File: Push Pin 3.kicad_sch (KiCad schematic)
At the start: 27 parts, among them J1 Screw_Terminal_01x02, J10 Screw_Terminal_01x02, J11 Screw_Terminal_01x02, J12 Screw_Terminal_01x02, J13 Screw_Terminal_01x02, J4 Screw_Terminal_01x02, J5 Screw_Terminal_01x02, J6 Screw_Terminal_01x02, J7 Screw_Terminal_01x02, J8 Screw_Terminal_01x02, J9 Screw_Terminal_01x02, SW1 SW_DPDT_x2, SW2 SW_DPDT_x2, SW3 SW_DPDT_x2, U1 LM2596S-ADJ

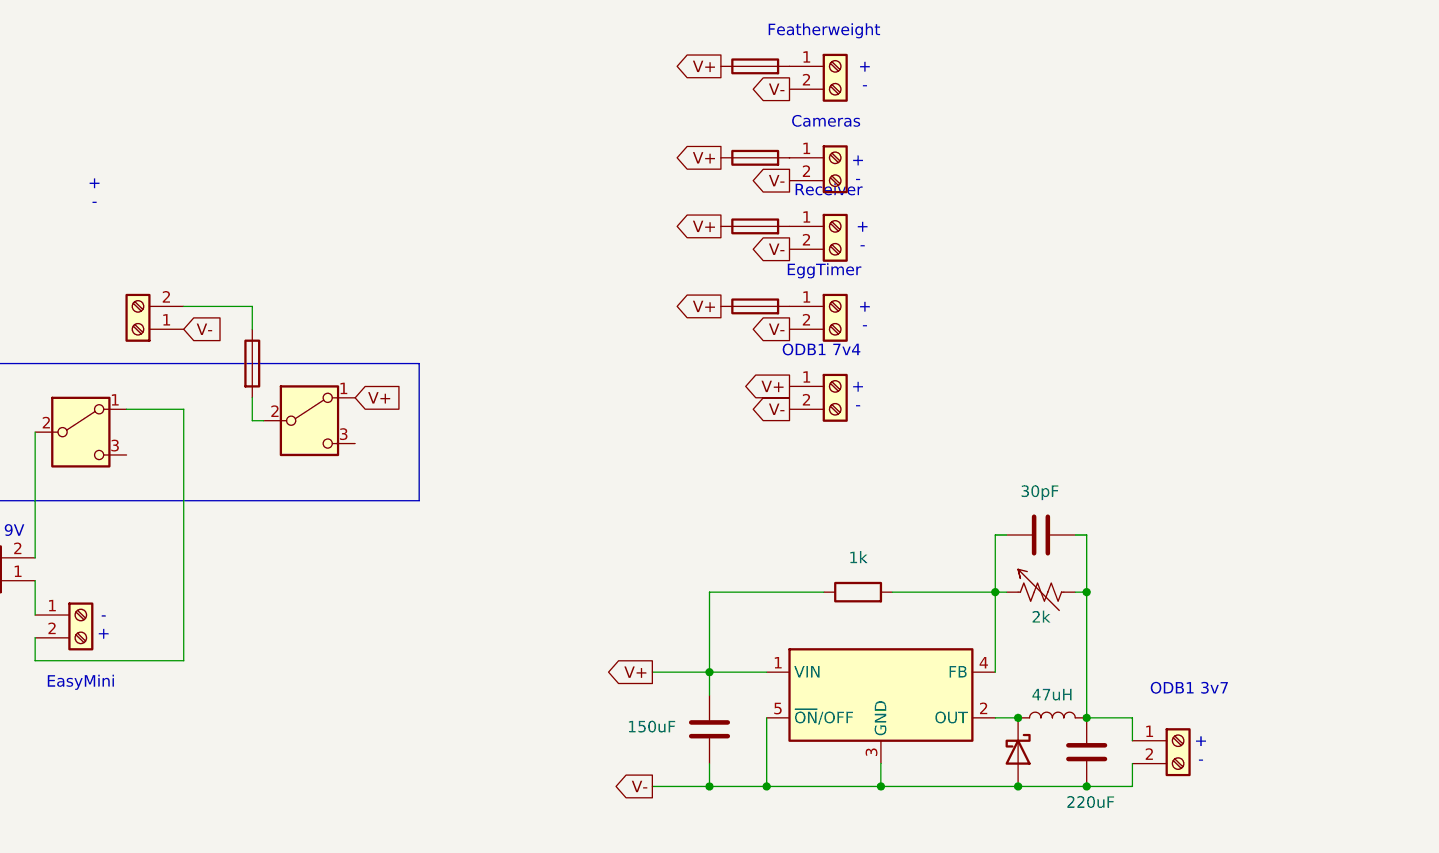
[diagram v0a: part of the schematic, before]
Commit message: Modifs des noms des nets
V+ à 7v4 et V- à GND
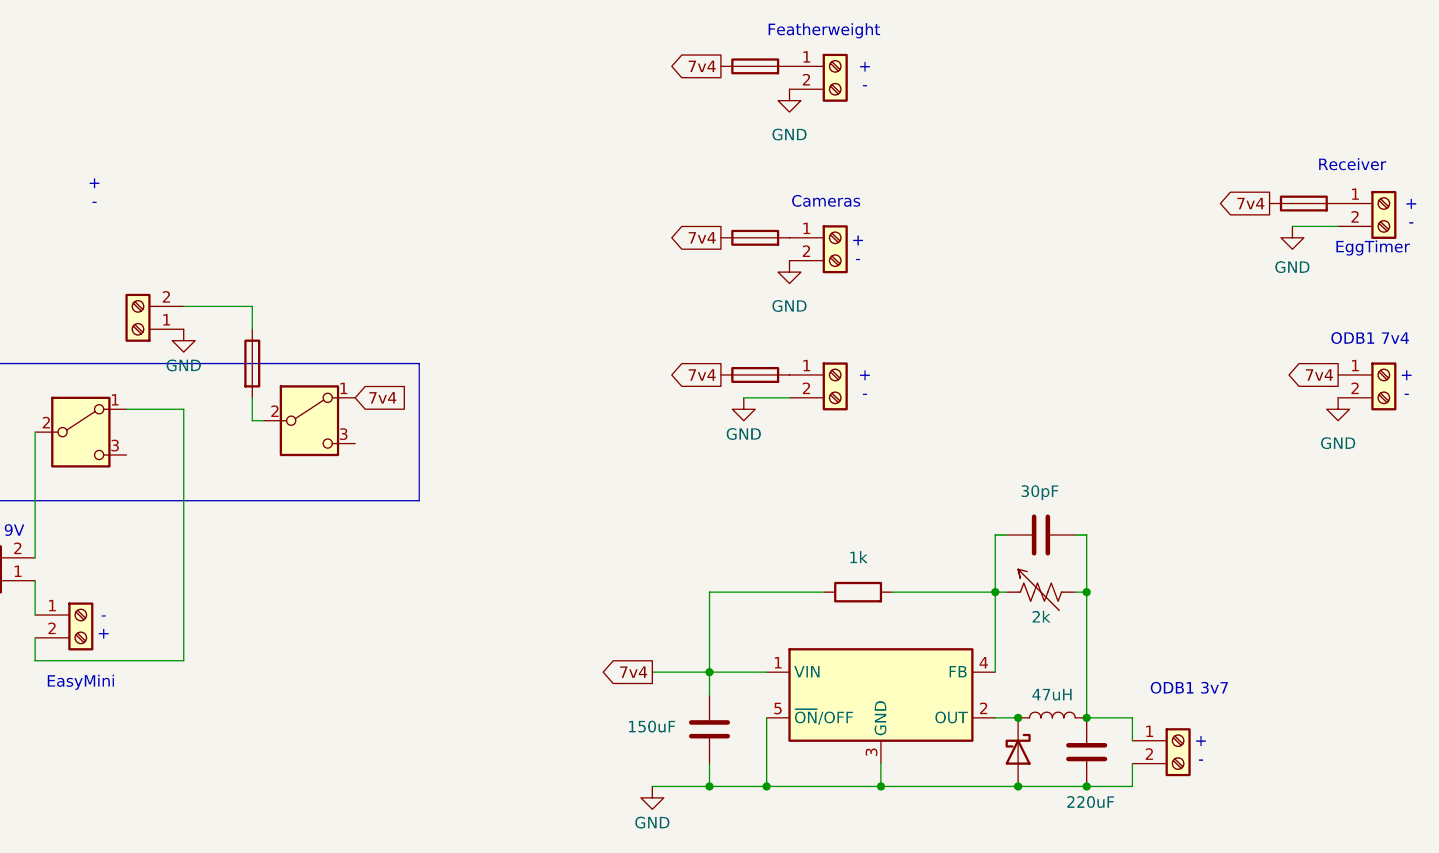
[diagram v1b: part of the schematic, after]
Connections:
- net V+ renamed 7v4
- net V- renamed GND

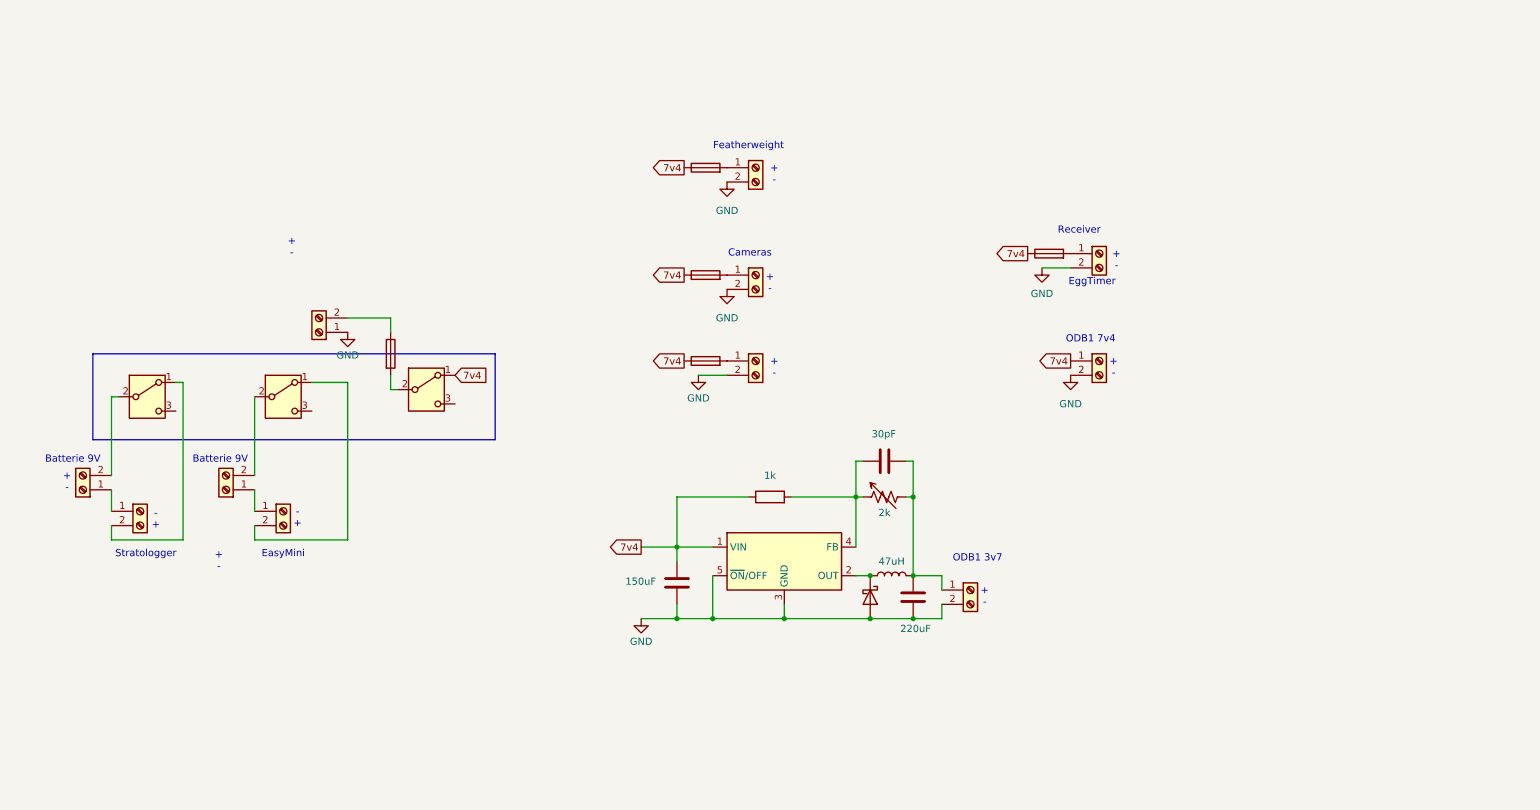
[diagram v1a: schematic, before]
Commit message: Modif circuits
Ajout des circuits de protection de polarité inverse
Commentaires capacités de découplage
Jumper pour joindre batteries
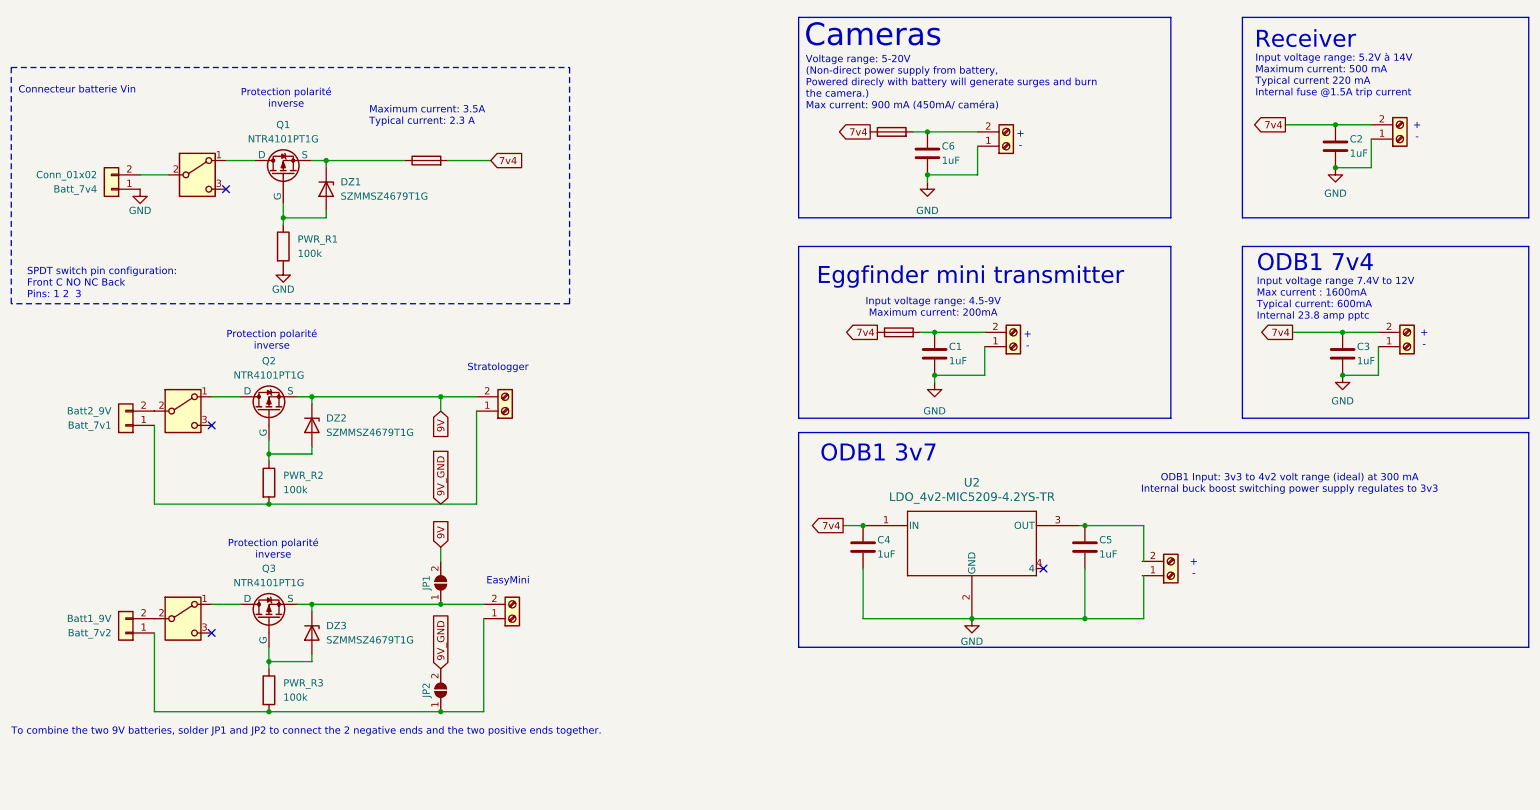
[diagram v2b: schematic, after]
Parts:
- removed D2: D_Schottky, Diode_SMD:Nexperia_CFP3_SOD-123W, symbol Device:D_Schottky
- removed F4, F5: Fuse, Fuse:Fuse_Bourns_MF-RHT050, symbol Device:Fuse
- removed J10, J11, J12, J13, J8, J9: Screw_Terminal_01x02, Connector_AMASS:AMASS_XT30U-M_1x02_P5.0mm_Vertical, symbol Connector:Screw_Terminal_01x02
- removed L1: 47uH, Inductor_SMD:L_0603_1608Metric, symbol Device:L
- removed R1: 1k, Resistor_SMD:R_0603_1608Metric, symbol Device:R
- removed R2: 2k, Potentiometer_SMD:Potentiometer_Bourns_3214G_Horizontal, symbol Device:R_Variable_US
- removed SW1, SW2, SW3: SW_DPDT_x2, Library:Omrun_SS-01GL13, symbol Switch:SW_DPDT_x2
- removed U1: LM2596S-ADJ, Package_TO_SOT_SMD:TO-263-5_TabPin3, symbol Regulator_Switching:LM2596S-ADJ
- added Batt_7v1: Batt2_9V, Connector_PinHeader_2.54mm:PinHeader_1x02_P2.54mm_Vertical, symbol Connector_Generic:Conn_01x02
- added Batt_7v2: Batt1_9V, Connector_PinHeader_2.54mm:PinHeader_1x02_P2.54mm_Vertical, symbol Connector_Generic:Conn_01x02
- added Batt_7v4: Conn_01x02, Connector_PinHeader_2.54mm:PinHeader_1x02_P2.54mm_Vertical, symbol Connector_Generic:Conn_01x02
- added C4, C5, C6: 1uF, Capacitor_SMD:C_1206_3216Metric, symbol Device:C
- added DZ1, DZ2, DZ3: SZMMSZ4679T1G, Diode_SMD:D_SOD-123, symbol Diode:BZV55C18
- added J2, J3: Screw_Terminal_01x02, Connector_AMASS:AMASS_XT30U-M_1x02_P5.0mm_Vertical, symbol Connector:Screw_Terminal_01x02
- added JP1, JP2: SolderJumper_2_Open, Jumper:SolderJumper-2_P1.3mm_Open_TrianglePad1.0x1.5mm, symbol Jumper:SolderJumper_2_Open
- added PWR_R1, PWR_R2, PWR_R3: 100k, Resistor_SMD:R_1206_3216Metric, symbol Device:R
- added Q1, Q2, Q3: NTR4101PT1G, Footprints:SOT-23, symbol Simulation_SPICE:PMOS
- added SW4, SW5, SW6: SW_DPDT_x2, Library:Omrun_SS-01GL13, symbol Switch:SW_DPDT_x2
- added U2: LDO_4v2-MIC5209-4.2YS-TR, SOT-223_S_MCH, symbol librairie_gaul:LDO_4v2-MIC5209-4.2YS-TR
- C1: value 220uF -> 1uF; footprint Capacitor_SMD:C_0603_1608Metric -> Capacitor_SMD:C_1206_3216Metric; Digikey (none) -> 1276-1068-1-ND
- C2: value 150uF -> 1uF; footprint Capacitor_SMD:C_0603_1608Metric -> Capacitor_SMD:C_1206_3216Metric; Digikey (none) -> 1276-1068-1-ND
- C3: value 30pF -> 1uF; footprint Capacitor_SMD:C_0603_1608Metric -> Capacitor_SMD:C_1206_3216Metric; Digikey (none) -> 1276-1068-1-ND
- F1: footprint Fuse:Fuse_Bourns_MF-RHT300 -> Fuse:Fuse_Bourns_MF-RHT070
- F3: footprint Fuse:Fuse_Bourns_MF-RHT050 -> Fuse:Fuse_Bourns_MF-RHT070
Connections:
- net 7v4: now also C3.1, F1.2, J4.2 (Pin_2), J6.2 (Pin_2), C4.1, U2.1 (IN)
- net GND: now also C3.2, J4.1 (Pin_1), J5.1 (Pin_1), J6.1 (Pin_1), Batt_7v4.1 (Pin_1), C4.2, C5.2, C6.2, PWR_R1.2, U2.2 (GND)
- net at C1.1: now also F3.2, J5.2 (Pin_2); no longer C3.2
- net at F1.1: now also DZ1.1 (K), Q1.3 (S); no longer J1.2 (Pin_2)
- net at F2.2: now also J1.2 (Pin_2), C6.1
- net at J7.1 (Pin_1): no longer J6.1 (Pin_1)
- new net: Q2.1 (D), SW5.1 (A)
- new net: Batt_7v1.2 (Pin_2), SW5.2 (B)
- new net: Q1.1 (D), SW4.1 (A)
- new net: Batt_7v4.2 (Pin_2), SW4.2 (B)
- new net: DZ3.2 (A), PWR_R3.1, Q3.2 (G)
- new net: Batt_7v2.1 (Pin_1), J3.1 (Pin_1), JP2.1 (A), PWR_R3.2
- new net: DZ1.2 (A), PWR_R1.1, Q1.2 (G)
- new net: C5.1, U2.3 (OUT)
- new net: DZ3.1 (K), J3.2 (Pin_2), JP1.1 (A), Q3.3 (S)
- new net: DZ2.2 (A), PWR_R2.1, Q2.2 (G)
- new net: Q3.1 (D), SW6.1 (A)
- new net: Batt_7v2.2 (Pin_2), SW6.2 (B)
- new net 9V: DZ2.1 (K), J2.2 (Pin_2), JP1.2 (B), Q2.3 (S)
- new net 9V_GND: Batt_7v1.1 (Pin_1), J2.1 (Pin_1), JP2.2 (B), PWR_R2.2
- no-connect marks 0 -> 4
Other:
- note added: "Connecteur batterie Vin"
- note added: "Eggfinder mini transmitter"
- note added: "Input voltage range 7.4V to 12V Max current : 1600mA Typical current: 600mA Internal 23.8 amp pptc"
- note added: "Input voltage range: 4.5-9V Maximum current: 200mA"
- note added: "Input voltage range: 5.2V à 14V Maximum current: 500 mA Typical current 220 mA Internal fuse @1.5A trip current"
- note added: "Maximum current: 3.5A Typical current: 2.3 A"
- note added: "ODB1 Input: 3v3 to 4v2 volt range (ideal) at 300 mA Internal buck boost switching power supply regulates to 3v3"
- note added: "Protection polarité inverse"
- note added: "SPDT switch pin configuration: Front C NO NC Back Pins: 1 2 3"
- note added: "To combine the two 9V batteries, solder JP1 and JP2 to connect the 2 negative ends and the two positive ends together."
- note added: "Voltage range: 5-20V (Non-direct power supply from battery, Powered direcly with battery will generate surges and burn the camera.) Max current: 900 mA (450mA/ caméra)"
- note removed: "- +"
- note removed: "Batterie 9V"
- note removed: "EggTimer"
- note removed: "Featherweight"

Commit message: PCB au complet
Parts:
- Batt_7v1, Batt_7v2, Batt_7v4: footprint Connector_PinHeader_2.54mm:PinHeader_1x02_P2.54mm_Vertical -> Connector_AMASS:AMASS_XT30U-M_1x02_P5.0mm_Vertical
- Q1, Q2, Q3: footprint Footprints:SOT-23 -> NTR4101PT1G:SOT-23-3_1P4X3P040_ONS
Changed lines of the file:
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@@
 			)
 		)
-		(property "Footprint" "Footprints:SOT-23"
+		(property "Footprint" "NTR4101PT1G:SOT-23-3_1P4X3P040_ONS"
 			(at 58.42 40.64 0)
 			(effects
@@
 			)
 		)
-		(property "Footprint" "Connector_PinHeader_2.54mm:PinHeader_1x02_P2.54mm_Vertical"
+		(property "Footprint" "Connector_AMASS:AMASS_XT30U-M_1x02_P5.0mm_Vertical"
 			(at 30.48 48.26 0)
 			(effects
@@
 			)
 		)
-		(property "Footprint" "Connector_PinHeader_2.54mm:PinHeader_1x02_P2.54mm_Vertical"
+		(property "Footprint" "Connector_AMASS:AMASS_XT30U-M_1x02_P5.0mm_Vertical"
 			(at 33.02 90.17 0)
 			(effects
@@
 			)
 		)
-		(property "Footprint" "Footprints:SOT-23"
+		(property "Footprint" "NTR4101PT1G:SOT-23-3_1P4X3P040_ONS"
 			(at 55.88 82.55 0)
 			(effects
@@
 			)
 		)
-		(property "Footprint" "Footprints:SOT-23"
+		(property "Footprint" "NTR4101PT1G:SOT-23-3_1P4X3P040_ONS"
 			(at 55.88 119.38 0)
 			(effects
@@
 			)
 		)
-		(property "Footprint" "Connector_PinHeader_2.54mm:PinHeader_1x02_P2.54mm_Vertical"
+		(property "Footprint" "Connector_AMASS:AMASS_XT30U-M_1x02_P5.0mm_Vertical"
 			(at 33.02 127 0)
 			(effects

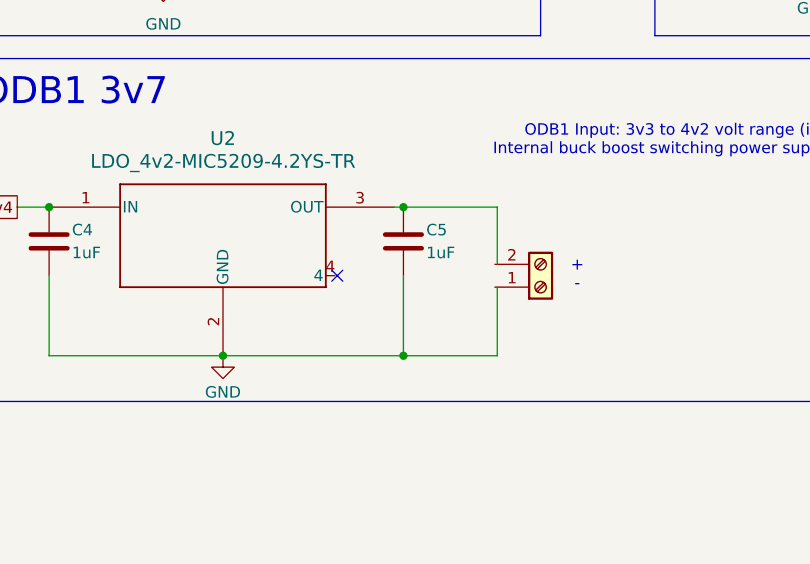
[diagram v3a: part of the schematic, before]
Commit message: Modifs silkscreen + odb1 3v7 connecteur
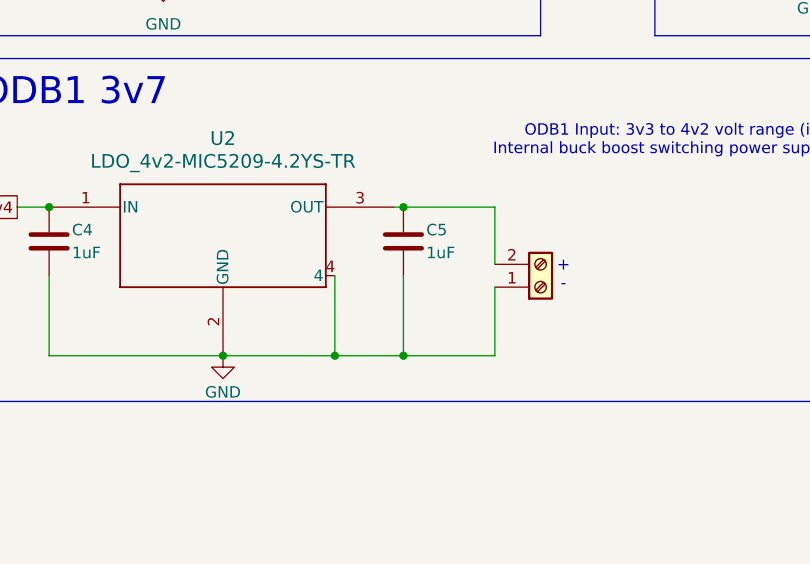
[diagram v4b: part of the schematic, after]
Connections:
- net GND: now also J7.1 (Pin_1), U2.4
- net at C5.1, U2.3 (OUT): now also J7.2 (Pin_2)
- no-connect marks 4 -> 3
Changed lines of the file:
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@@
+	)
+	(junction
+		(at 195.58 124.46)
+		(diameter 0)
+		(color 0 0 0 0)
 	)
 	(junction
@@
 	)
 	(no_connect
-		(at 195.85 115.57)
-	)
-	(no_connect
 		(at 48.26 127)
 	)
@@
 	(wire
 		(pts
-			(xy 213.63 107.95) (xy 213.63 114.3)
+			(xy 213.36 107.95) (xy 213.36 114.3)
 		)
 		(stroke
@@
 	(wire
 		(pts
-			(xy 183.15 124.46) (xy 203.2 124.46)
-		)
-		(stroke
-			(width 0)
-			(type default)
-		)
-	)
-	(wire
-		(pts
-			(xy 213.63 116.84) (xy 213.63 124.46)
+			(xy 183.15 124.46) (xy 195.58 124.46)
+		)
+		(stroke
+			(width 0)
+			(type default)
+		)
+	)
+	(wire
+		(pts
+			(xy 213.36 116.84) (xy 213.36 124.46)
 		)
 		(stroke
@@
 	(wire
 		(pts
-			(xy 203.2 124.46) (xy 213.63 124.46)
+			(xy 203.2 124.46) (xy 213.36 124.46)
 		)
 		(stroke
@@
 	(wire
 		(pts
-			(xy 203.2 107.95) (xy 213.63 107.95)
+			(xy 203.2 107.95) (xy 213.36 107.95)
+		)
+		(stroke
+			(width 0)
+			(type default)
+		)
+	)
+	(wire
+		(pts
+			(xy 195.58 124.46) (xy 203.2 124.46)
 		)
 		(stroke
@@
 		(pts
 			(xy 176.53 73.66) (xy 185.42 73.66)
+		)
+		(stroke
+			(width 0)
+			(type default)
+		)
+	)
+	(wire
+		(pts
+			(xy 195.58 115.57) (xy 195.58 124.46)
 		)
 		(stroke
@@
 	(text "+\n-\n"
 		(exclude_from_sim no)
-		(at 222.52 115.57 0)
+		(at 220.98 115.57 0)
 		(effects
 			(font

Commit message: Plus beau
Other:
- moved on the sheet: Batt_7v4, DZ1, PWR_R1, Q1
